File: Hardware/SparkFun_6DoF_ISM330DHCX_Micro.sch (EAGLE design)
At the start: 27 parts, among them U1 ISM330DHCX

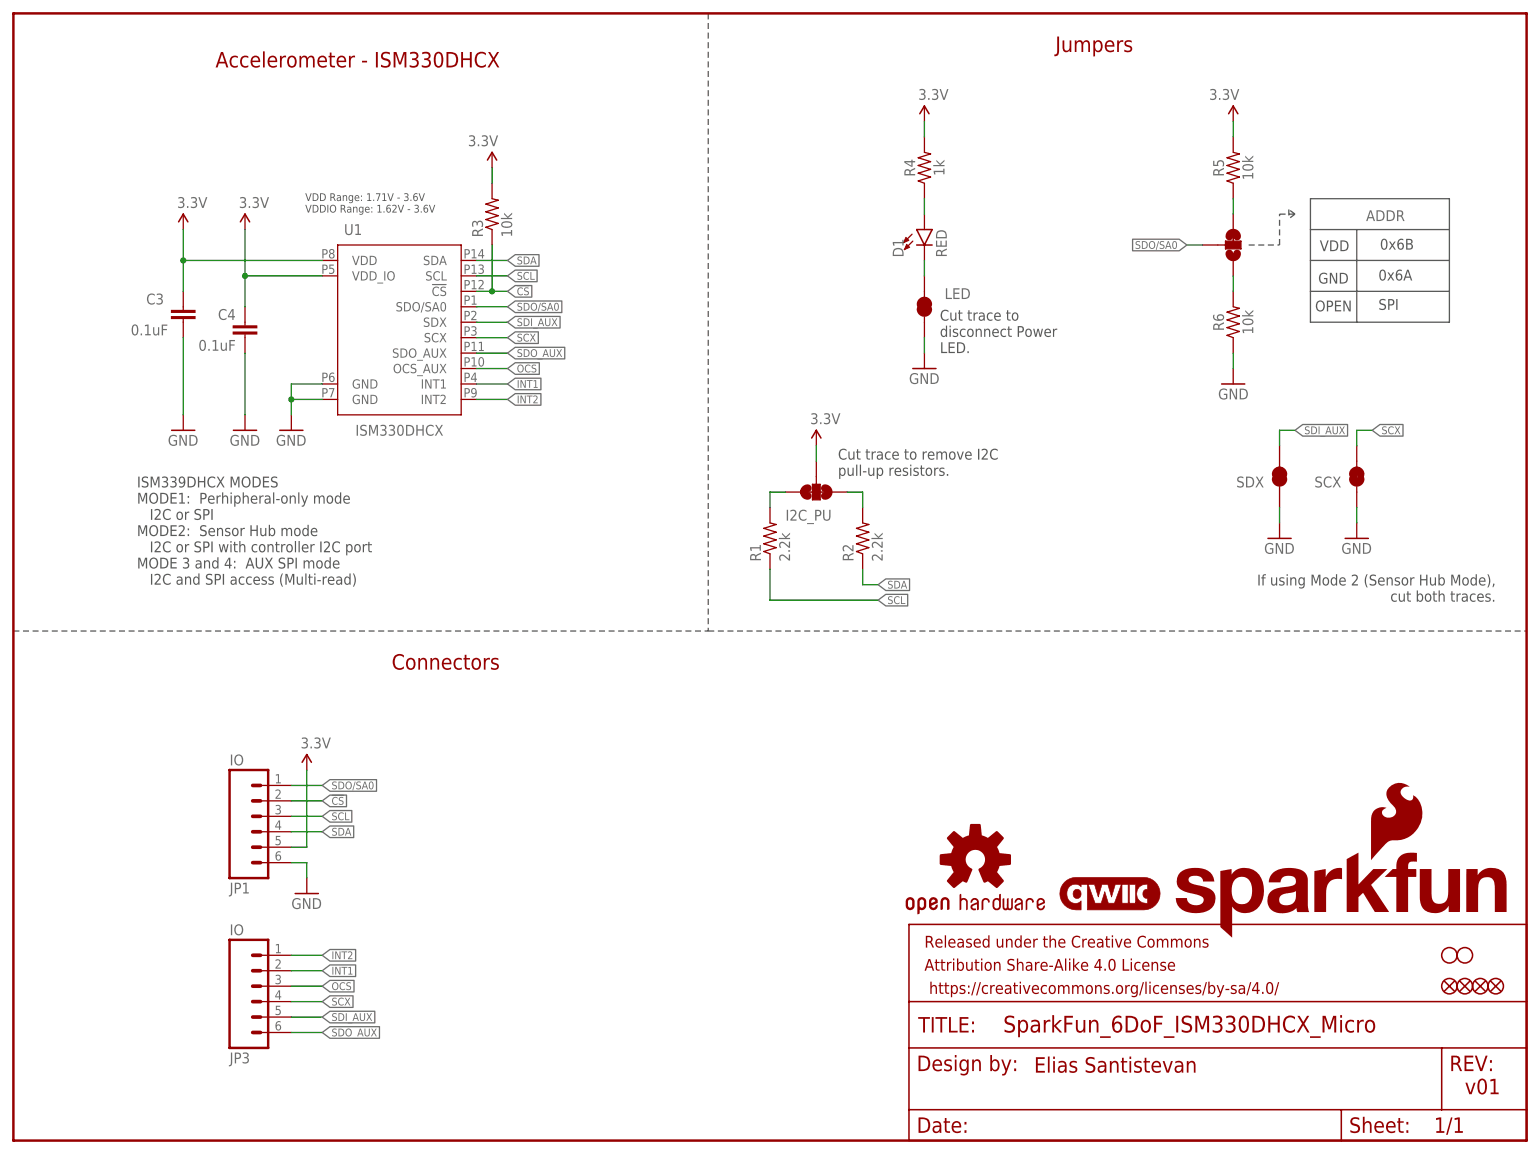
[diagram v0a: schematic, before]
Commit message: Adds labels to Mini
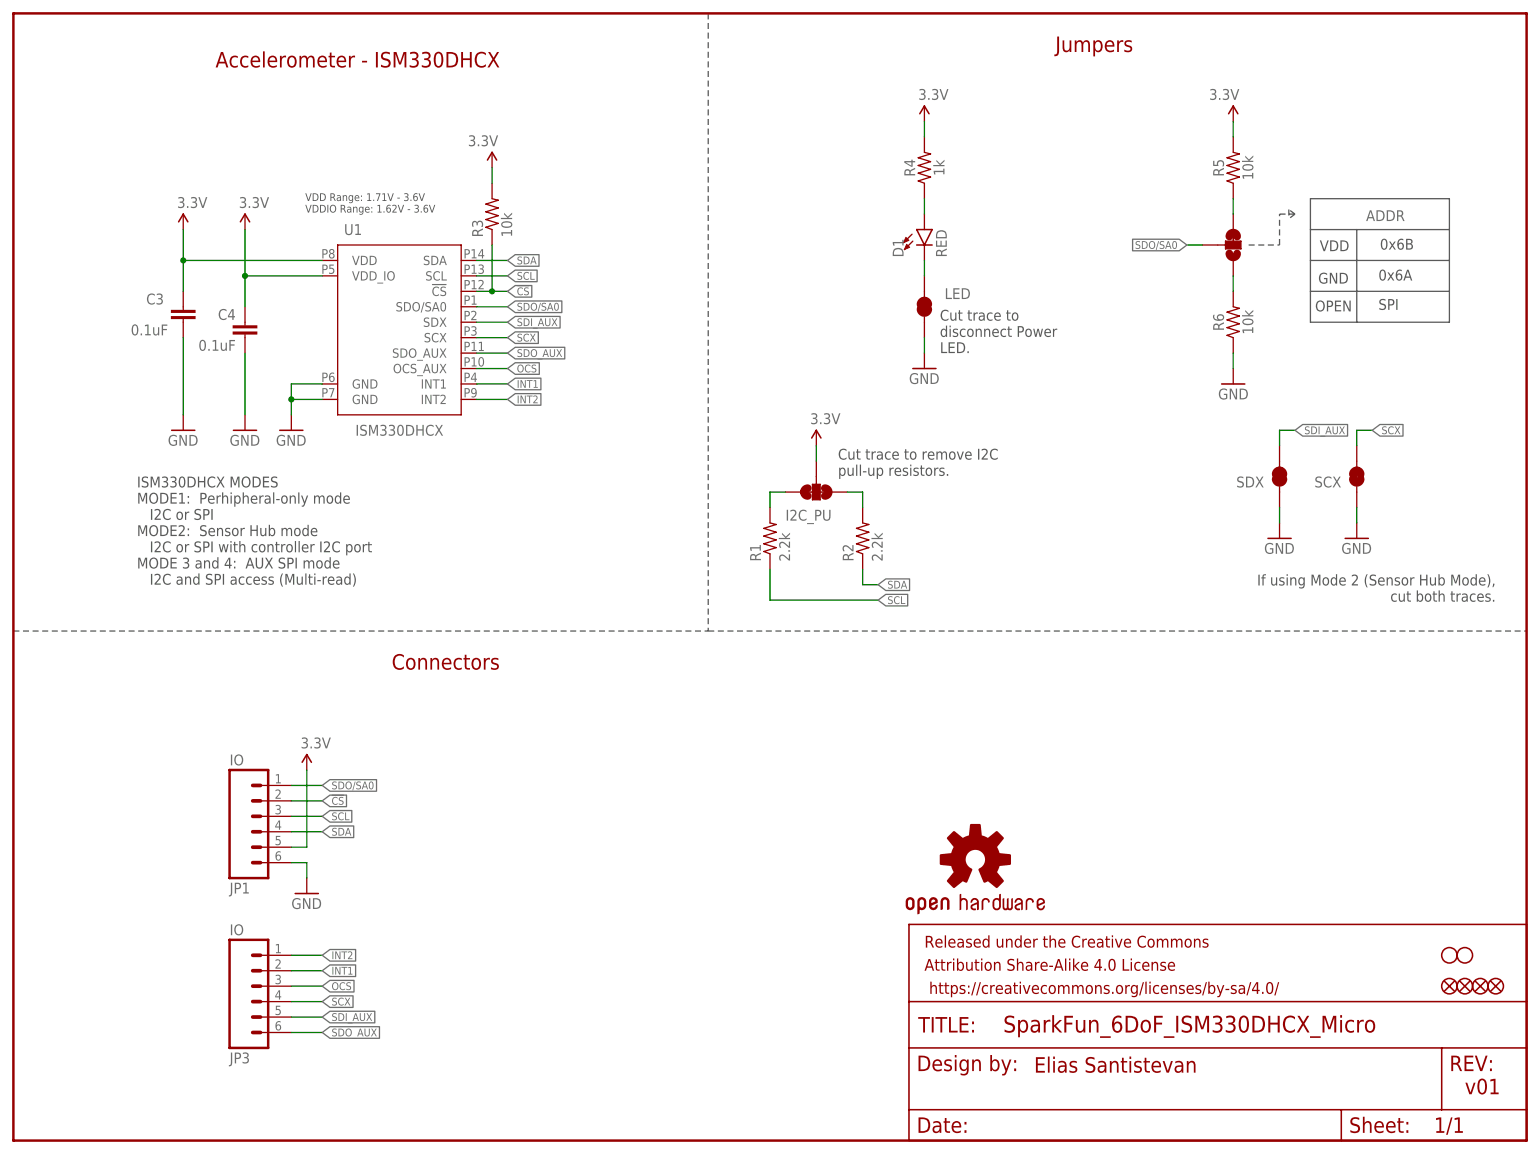
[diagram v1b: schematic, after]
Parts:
- removed LOGO1: QWIIC_LOGO_4MM, SparkFun-Aesthetics:QWIIC_LOGO_4MM
- removed LOGO3: SFE_LOGO_NAME_FLAME.1_INCH, SparkFun-Aesthetics:SFE_LOGO_NAME_FLAME.1_INCH
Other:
- note added: "ISM330DHCX MODES MODE1: Perhipheral-only mode I2C or SPI MODE2: Sensor Hub mode I2C or SPI with controller I2C port MODE 3 and 4: AUX SPI mode I2C and SPI access (Multi-read)"
- note removed: "ISM339DHCX MODES MODE1: Perhipheral-only mode I2C or SPI MODE2: Sensor Hub mode I2C or SPI with controller I2C port MODE 3 and 4: AUX SPI mode I2C and SPI access (Multi-read)"
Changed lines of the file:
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@@
 <part name="SDX" library="SparkFun-Jumpers" deviceset="JUMPER-SMT_2_NC_TRACE" device="_SILK" package3d_urn="urn:adsk.eagle:package:39281/1"/>
 <part name="SCX" library="SparkFun-Jumpers" deviceset="JUMPER-SMT_2_NC_TRACE" device="_SILK" package3d_urn="urn:adsk.eagle:package:39281/1"/>
-<part name="LOGO3" library="SparkFun-Aesthetics" deviceset="SFE_LOGO_NAME_FLAME" device=".1_INCH" value="SFE_LOGO_NAME_FLAME.1_INCH"/>
 <part name="JP3" library="SparkFun-Connectors" deviceset="CONN_06" device="NO_SILK_NO_POP" value="IO"/>
 <part name="FD1" library="SparkFun-Aesthetics" deviceset="FIDUCIAL" device="UFIDUCIAL"/>
 <part name="FD2" library="SparkFun-Aesthetics" deviceset="FIDUCIAL" device="UFIDUCIAL"/>
-<part name="LOGO1" library="SparkFun-Aesthetics" deviceset="QWIIC_LOGO" device="_4MM" value="QWIIC_LOGO_4MM"/>
 <part name="D1" library="SparkFun-LED" deviceset="LED-RED" device="0603" value="RED"/>
 <part name="R4" library="SparkFun-Resistors" deviceset="1KOHM" device="-0402T-1/16W-1%" value="1k"/>
@@
 <text x="135.636" y="113.792" size="1.778" layer="97" font="vector" align="top-left">Cut trace to remove I2C
 pull-up resistors.</text>
-<text x="20.32" y="109.22" size="1.778" layer="97" font="vector" align="top-left">ISM339DHCX MODES
+<text x="20.32" y="109.22" size="1.778" layer="97" font="vector" align="top-left">ISM330DHCX MODES
 MODE1:  Perhipheral-only mode
    I2C or SPI
@@
 <attribute name="NAME" x="218.44" y="109.22" size="1.778" layer="95" font="vector" rot="R180"/>
 </instance>
-<instance part="LOGO3" gate="G$1" x="190.5" y="33.02" smashed="yes"/>
 <instance part="JP3" gate="G$1" x="40.64" y="25.4" smashed="yes" rot="MR180">
 <attribute name="VALUE" x="35.56" y="35.56" size="1.778" layer="96" font="vector" rot="MR180"/>
@@
 <instance part="FD1" gate="G$1" x="241.3" y="25.4" smashed="yes"/>
 <instance part="FD2" gate="G$1" x="243.84" y="25.4" smashed="yes"/>
-<instance part="LOGO1" gate="G$1" x="180.34" y="40.64" smashed="yes"/>
 <instance part="D1" gate="G$1" x="149.86" y="149.86" smashed="yes">
 <attribute name="NAME" x="146.431" y="145.288" size="1.778" layer="95" font="vector" rot="R90"/>
